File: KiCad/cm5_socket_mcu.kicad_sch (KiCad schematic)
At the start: 6 parts, among them IC1 AZ1117CH2-3.3TRG1, IC2 PI3USB102ZLEX

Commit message: #15
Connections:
- net USB3_1_D+: now reaches SoM1.163 (USB3-1-DP)
- net USB3_1_D+: now also IC2.7 (D+)
- net USB3_1_D-: now reaches SoM1.165 (USB3-1-DM)
- net USB3_1_D-: now also IC2.6 (D-)
- net USB3_1+: no longer names the net of SoM1.171 (USB3-1-TX_P)
- net USB3_1+: no longer IC2.7 (D+)
- net USB3_1-: no longer names the net of SoM1.169 (USB3-1-TX_N)
- net USB3_1-: no longer IC2.6 (D-)
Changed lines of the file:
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@@
 	(title_block
 		(title "${project_name}")
-		(date "2026-03-26")
+		(date "2026-03-28")
 		(rev "${project_version}")
 		(company "${project_creator}")
@@
 	)
 	(no_connect
+		(at 205.74 114.3)
+	)
+	(no_connect
 		(at 50.8 45.72)
 	)
@@
 	)
 	(no_connect
+		(at 205.74 111.76)
+	)
+	(no_connect
 		(at 205.74 129.54)
 	)
@@
 	)
 	(no_connect
-		(at 205.74 106.68)
-	)
-	(no_connect
 		(at 205.74 96.52)
-	)
-	(no_connect
-		(at 205.74 104.14)
 	)
 	(no_connect
@@
 	(wire
 		(pts
-			(xy 226.06 58.42) (xy 226.06 111.76)
+			(xy 226.06 58.42) (xy 226.06 106.68)
 		)
 		(stroke
@@
 	(wire
 		(pts
-			(xy 205.74 111.76) (xy 226.06 111.76)
-		)
-		(stroke
-			(width 0)
-			(type default)
-		)
-	)
-	(wire
-		(pts
 			(xy 205.74 93.98) (xy 208.28 93.98)
 		)
@@
 	(wire
 		(pts
+			(xy 205.74 104.14) (xy 228.6 104.14)
+		)
+		(stroke
+			(width 0)
+			(type default)
+		)
+	)
+	(wire
+		(pts
 			(xy 48.26 147.32) (xy 50.8 147.32)
 		)
@@
 	(wire
 		(pts
-			(xy 205.74 114.3) (xy 228.6 114.3)
-		)
-		(stroke
-			(width 0)
-			(type default)
-		)
-	)
-	(wire
-		(pts
 			(xy 78.74 175.26) (xy 68.58 175.26)
 		)
@@
 	(wire
 		(pts
+			(xy 205.74 106.68) (xy 226.06 106.68)
+		)
+		(stroke
+			(width 0)
+			(type default)
+		)
+	)
+	(wire
+		(pts
 			(xy 205.74 124.46) (xy 208.28 124.46)
 		)
@@
 	(wire
 		(pts
-			(xy 228.6 60.96) (xy 228.6 114.3)
+			(xy 228.6 60.96) (xy 228.6 104.14)
 		)
 		(stroke
@@
 		)
 	)
-	(label "USB3_1-"
+	(label "USB3_1_D-"
 		(at 228.6 58.42 0)
 		(effects
@@
 		)
 	)
-	(label "USB3_1+"
+	(label "USB3_1_D+"
 		(at 228.6 60.96 0)
 		(effects

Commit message: #16
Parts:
- renumbered C3 to C1, C1 to C2, C2 to C3, IC2 to IC1, IC1 to IC2
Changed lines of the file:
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@@
 		(on_board yes)
 		(dnp no)
-		(property "Reference" "#PWR010"
+		(property "Reference" "#PWR01"
 			(at 241.3 74.93 0)
 			(effects
@@
 			(project "BB3plus CM5 STM32H7 module"
 				(path "/1a4f0aea-3a69-423f-8790-3103cd0321c4/c2910023-6066-4877-a406-045757318a99"
-					(reference "#PWR010")
+					(reference "#PWR01")
 					(unit 1)
 				)
@@
 		(on_board yes)
 		(dnp no)
-		(property "Reference" "#PWR07"
+		(property "Reference" "#PWR06"
 			(at 104.14 161.29 0)
 			(effects
@@
 			(project "BB3plus CM5 STM32H7 module"
 				(path "/1a4f0aea-3a69-423f-8790-3103cd0321c4/c2910023-6066-4877-a406-045757318a99"
-					(reference "#PWR07")
+					(reference "#PWR06")
 					(unit 1)
 				)
@@
 		(dnp no)
 		(fields_autoplaced yes)
-		(property "Reference" "IC1"
+		(property "Reference" "IC2"
 			(at 38.1 172.085 0)
 			(do_not_autoplace yes)
@@
 			(project ""
 				(path "/1a4f0aea-3a69-423f-8790-3103cd0321c4/c2910023-6066-4877-a406-045757318a99"
-					(reference "IC1")
+					(reference "IC2")
 					(unit 1)
 				)
@@
 		(on_board yes)
 		(dnp no)
-		(property "Reference" "#PWR01"
+		(property "Reference" "#PWR09"
 			(at 30.48 189.23 0)
 			(effects
@@
 			(project "BB3plus CM5 STM32H7 module"
 				(path "/1a4f0aea-3a69-423f-8790-3103cd0321c4/c2910023-6066-4877-a406-045757318a99"
-					(reference "#PWR01")
+					(reference "#PWR09")
 					(unit 1)
 				)
@@
 		(on_board yes)
 		(dnp no)
-		(property "Reference" "#PWR02"
+		(property "Reference" "#PWR03"
 			(at 41.91 134.62 0)
 			(effects
@@
 			(project "BB3plus CM5 STM32H7 module"
 				(path "/1a4f0aea-3a69-423f-8790-3103cd0321c4/c2910023-6066-4877-a406-045757318a99"
-					(reference "#PWR02")
+					(reference "#PWR03")
 					(unit 1)
 				)
@@
 		(on_board yes)
 		(dnp no)
-		(property "Reference" "#PWR09"
+		(property "Reference" "#PWR08"
 			(at 208.28 161.29 0)
 			(effects
@@
 			(project "BB3plus CM5 STM32H7 module"
 				(path "/1a4f0aea-3a69-423f-8790-3103cd0321c4/c2910023-6066-4877-a406-045757318a99"
-					(reference "#PWR09")
+					(reference "#PWR08")
 					(unit 1)
 				)
@@
 		(on_board yes)
 		(dnp no)
-		(property "Reference" "#+3V03"
+		(property "Reference" "#+3V01"
 			(at 241.3 40.64 0)
 			(effects
@@
 			(project "BB3plus CM5 STM32H7 module"
 				(path "/1a4f0aea-3a69-423f-8790-3103cd0321c4/c2910023-6066-4877-a406-045757318a99"
-					(reference "#+3V03")
+					(reference "#+3V01")
 					(unit 1)
 				)
@@
 		(on_board yes)
 		(dnp no)
-		(property "Reference" "C3"
+		(property "Reference" "C1"
 			(at 236.22 45.085 90)
 			(effects
@@
 			(project "BB3plus CM5 STM32H7 module"
 				(path "/1a4f0aea-3a69-423f-8790-3103cd0321c4/c2910023-6066-4877-a406-045757318a99"
-					(reference "C3")
+					(reference "C1")
 					(unit 1)
 				)
@@
 		(on_board yes)
 		(dnp no)
-		(property "Reference" "#+3V01"
+		(property "Reference" "#+3V02"
 			(at 38.1 129.54 0)
 			(effects
@@
 			(project "BB3plus CM5 STM32H7 module"
 				(path "/1a4f0aea-3a69-423f-8790-3103cd0321c4/c2910023-6066-4877-a406-045757318a99"
-					(reference "#+3V01")
+					(reference "#+3V02")
 					(unit 1)
 				)
@@
 		(on_board yes)
 		(dnp no)
-		(property "Reference" "IC2"
+		(property "Reference" "IC1"
 			(at 246.38 45.085 0)
 			(do_not_autoplace yes)
@@
 			(project ""
 				(path "/1a4f0aea-3a69-423f-8790-3103cd0321c4/c2910023-6066-4877-a406-045757318a99"
-					(reference "IC2")
+					(reference "IC1")
 					(unit 1)
 				)
@@
 		(on_board yes)
 		(dnp no)
-		(property "Reference" "#FLG01"
+		(property "Reference" "#FLG02"
 			(at 43.18 117.475 0)
 			(effects
@@
 			(project "BB3plus CM5 STM32H7 module"
 				(path "/1a4f0aea-3a69-423f-8790-3103cd0321c4/c2910023-6066-4877-a406-045757318a99"
-					(reference "#FLG01")
+					(reference "#FLG02")
 					(unit 1)
 				)
@@
 		(on_board yes)
 		(dnp no)
-		(property "Reference" "#PWR05"
+		(property "Reference" "#PWR011"
 			(at 68.58 189.23 0)
 			(effects
@@
 			(project "BB3plus CM5 STM32H7 module"
 				(path "/1a4f0aea-3a69-423f-8790-3103cd0321c4/c2910023-6066-4877-a406-045757318a99"
-					(reference "#PWR05")
+					(reference "#PWR011")
 					(unit 1)
 				)
@@
 		(on_board yes)
 		(dnp no)
-		(property "Reference" "C1"
+		(property "Reference" "C2"
 			(at 30.988 177.9524 0)
 			(effects
@@
 			(project "BB3plus CM5 STM32H7 module"
 				(path "/1a4f0aea-3a69-423f-8790-3103cd0321c4/c2910023-6066-4877-a406-045757318a99"
-					(reference "C1")
+					(reference "C2")
 					(unit 1)
 				)
@@
 		(on_board yes)
 		(dnp no)
-		(property "Reference" "#PWR04"
+		(property "Reference" "#PWR010"
 			(at 60.96 189.23 0)
 			(effects
@@
 			(project "BB3plus CM5 STM32H7 module"
 				(path "/1a4f0aea-3a69-423f-8790-3103cd0321c4/c2910023-6066-4877-a406-045757318a99"
-					(reference "#PWR04")
+					(reference "#PWR010")
 					(unit 1)
 				)
@@
 		(on_board yes)
 		(dnp no)
-		(property "Reference" "#+5V01"
+		(property "Reference" "#+5V02"
 			(at 25.4 175.26 0)
 			(effects
@@
 			(project ""
 				(path "/1a4f0aea-3a69-423f-8790-3103cd0321c4/c2910023-6066-4877-a406-045757318a99"
-					(reference "#+5V01")
+					(reference "#+5V02")
 					(unit 1)
 				)
@@
 		(on_board yes)
 		(dnp no)
-		(property "Reference" "#PWR011"
+		(property "Reference" "#PWR02"
 			(at 266.7 74.93 0)
 			(effects
@@
 			(project "BB3plus CM5 STM32H7 module"
 				(path "/1a4f0aea-3a69-423f-8790-3103cd0321c4/c2910023-6066-4877-a406-045757318a99"
-					(reference "#PWR011")
+					(reference "#PWR02")
 					(unit 1)
 				)
@@
 		(on_board yes)
 		(dnp no)
-		(property "Reference" "#PWR03"
+		(property "Reference" "#PWR04"
 			(at 48.26 161.29 0)
 			(effects
@@
 			(project "BB3plus CM5 STM32H7 module"
 				(path "/1a4f0aea-3a69-423f-8790-3103cd0321c4/c2910023-6066-4877-a406-045757318a99"
-					(reference "#PWR03")
+					(reference "#PWR04")
 					(unit 1)
 				)
@@
 		(on_board yes)
 		(dnp no)
-		(property "Reference" "#PWR08"
+		(property "Reference" "#PWR07"
 			(at 147.32 161.29 0)
 			(effects
@@
 			(project "BB3plus CM5 STM32H7 module"
 				(path "/1a4f0aea-3a69-423f-8790-3103cd0321c4/c2910023-6066-4877-a406-045757318a99"
-					(reference "#PWR08")
+					(reference "#PWR07")
 					(unit 1)
 				)
@@
 		(on_board yes)
 		(dnp no)
-		(property "Reference" "#PWR06"
+		(property "Reference" "#PWR05"
 			(at 76.2 161.29 0)
 			(effects
@@
 			(project "BB3plus CM5 STM32H7 module"
 				(path "/1a4f0aea-3a69-423f-8790-3103cd0321c4/c2910023-6066-4877-a406-045757318a99"
-					(reference "#PWR06")
+					(reference "#PWR05")
 					(unit 1)
 				)
@@
 		(on_board yes)
 		(dnp no)
-		(property "Reference" "#+3V02"
+		(property "Reference" "#+3V03"
 			(at 81.28 175.26 0)
 			(effects
@@
 			(project "BB3plus CM5 STM32H7 module"
 				(path "/1a4f0aea-3a69-423f-8790-3103cd0321c4/c2910023-6066-4877-a406-045757318a99"
-					(reference "#+3V02")
+					(reference "#+3V03")
 					(unit 1)
 				)
@@
 		(on_board yes)
 		(dnp no)
-		(property "Reference" "C2"
+		(property "Reference" "C3"
 			(at 69.088 177.9524 0)
 			(effects
@@
 			(project "BB3plus CM5 STM32H7 module"
 				(path "/1a4f0aea-3a69-423f-8790-3103cd0321c4/c2910023-6066-4877-a406-045757318a99"
-					(reference "C2")
+					(reference "C3")
 					(unit 1)
 				)
@@
 		(on_board yes)
 		(dnp no)
-		(property "Reference" "#FLG02"
+		(property "Reference" "#FLG01"
 			(at 48.26 23.495 0)
 			(effects
@@
 			(project "BB3plus CM5 STM32H7 module"
 				(path "/1a4f0aea-3a69-423f-8790-3103cd0321c4/c2910023-6066-4877-a406-045757318a99"
-					(reference "#FLG02")
+					(reference "#FLG01")
 					(unit 1)
 				)
@@
 		(on_board yes)
 		(dnp no)
-		(property "Reference" "#+5V02"
+		(property "Reference" "#+5V01"
 			(at 114.3 121.92 0)
 			(effects
@@
 			(project "BB3plus CM5 STM32H7 module"
 				(path "/1a4f0aea-3a69-423f-8790-3103cd0321c4/c2910023-6066-4877-a406-045757318a99"
-					(reference "#+5V02")
+					(reference "#+5V01")
 					(unit 1)
 				)

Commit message: #18, OSHW ID121
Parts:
- added C4: 1u, PCM_EEZ_passives:C_0402_1005Metric, symbol PCM_EEZ_passives:C-EU
- added C5: 10u, PCM_EEZ_passives:C_0603_1608Metric, symbol PCM_EEZ_passives:C-EU
- added IC3: AZ1117CH-1.8TRG1, PCM_EEZ_SMD:SOT223, symbol PCM_EEZ_ICs:AZ1117CH2-3.3TRG1
- C1: LCSC (none) -> C60474
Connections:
- net +1V8: now also C5.2, IC3.3 (OUTPUT)
- net +3V3: now also C4.1, IC3.1 (INPUT)
- net GND: now also C4.2, C5.1, IC3.2 (ADJ/GND), IC3.4 (ADJ/GND)
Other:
- note added: "+1V8 LDO (max 1A)"

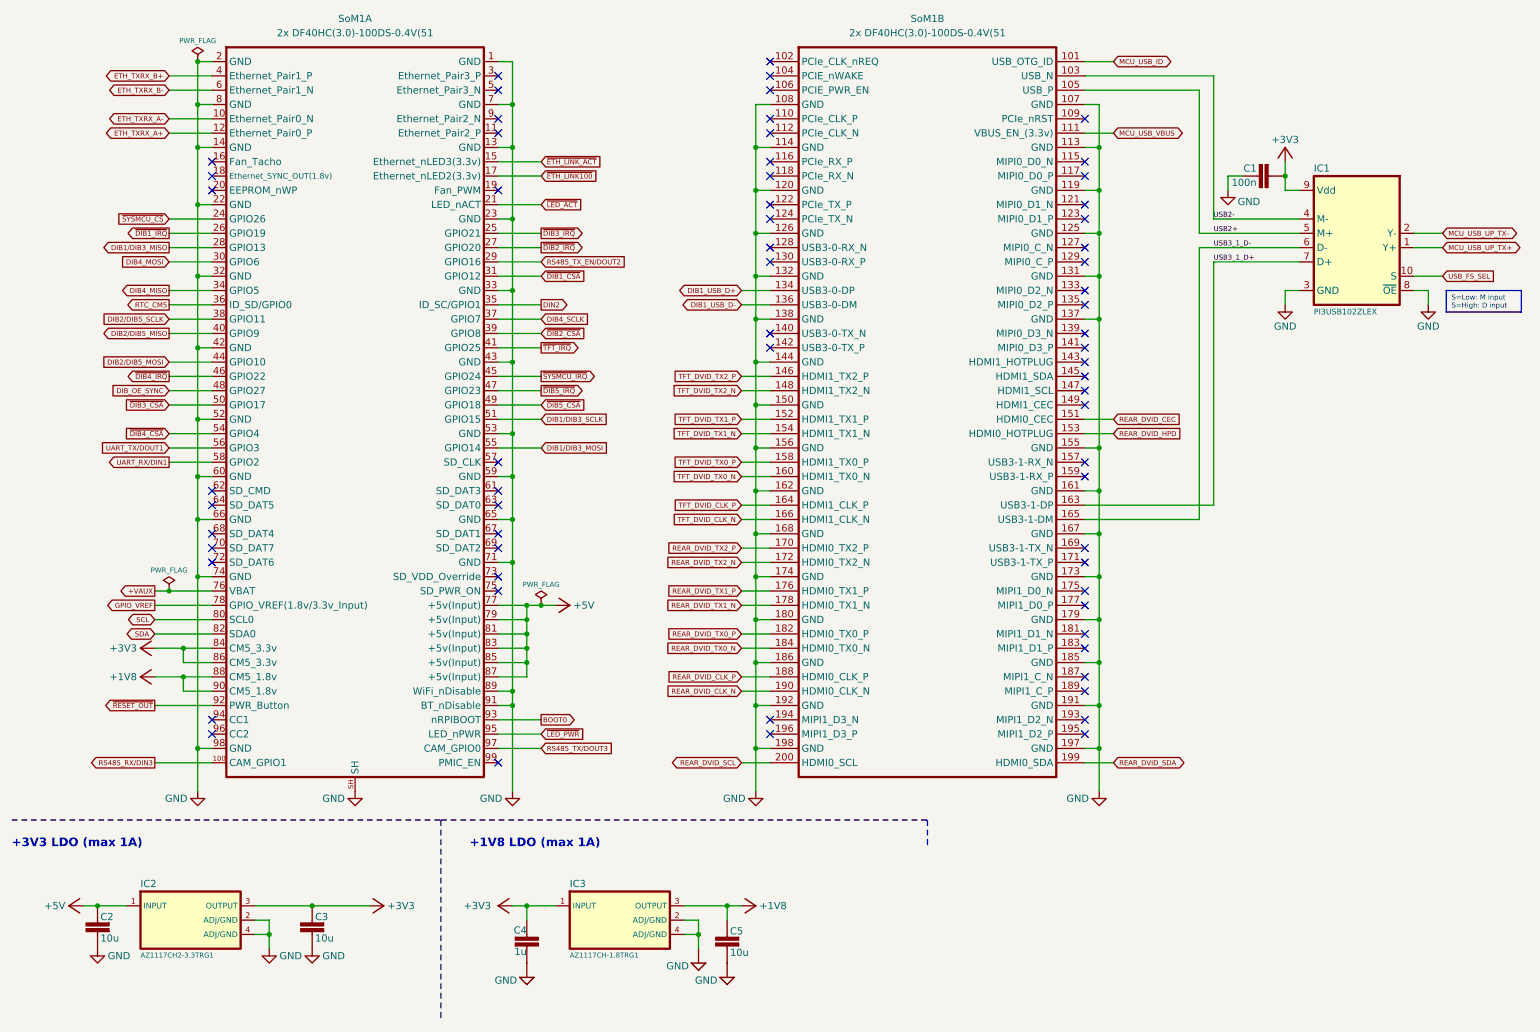
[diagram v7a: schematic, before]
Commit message: USB lanes renamed, OSHWA logo added
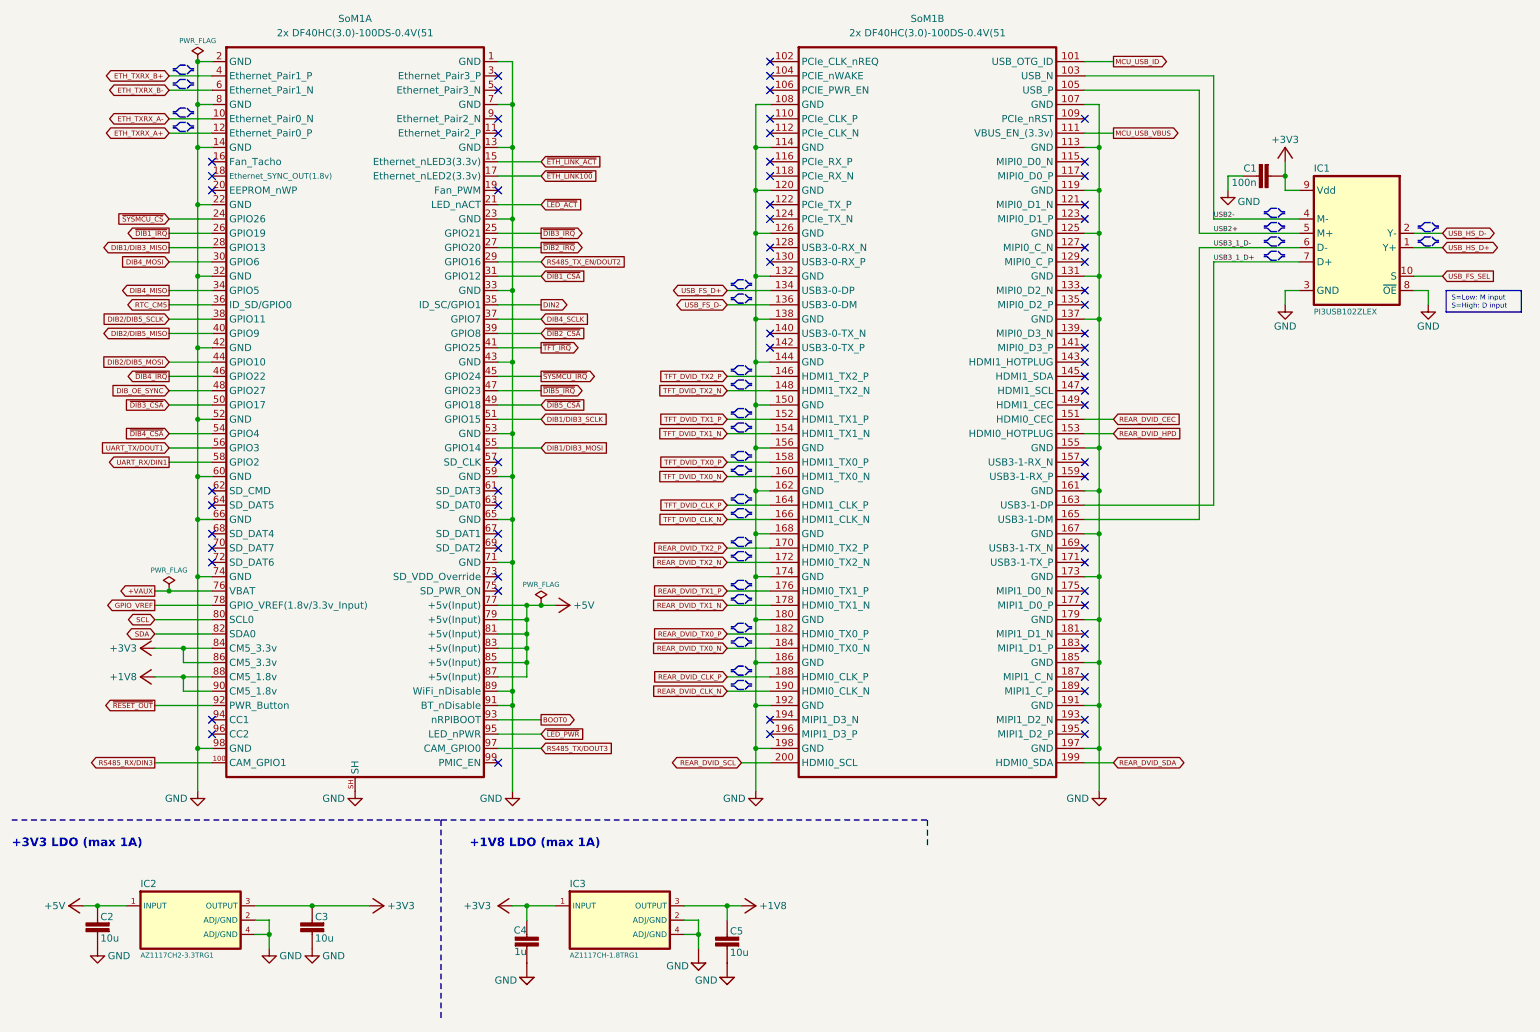
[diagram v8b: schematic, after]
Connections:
- net DIB1_USB_D+ renamed USB_FS_D+
- net DIB1_USB_D- renamed USB_FS_D-
- net MCU_USB_UP_TX+ renamed USB_HS_D+
- net MCU_USB_UP_TX- renamed USB_HS_D-
